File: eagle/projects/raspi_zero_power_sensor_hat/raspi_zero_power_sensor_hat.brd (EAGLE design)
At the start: 65 x 30 mm, 155 parts, among them J301 MOL-SL-2-RA, J302 USB_MICROB_RECPT, J401 MOL-SL-2-RA, J402 MOL-SL-2-V, J601 RECEPTACLE-2x5-2.54MM, J602 MOL-SL-4-RA, J603 MOL-SL-3-V, J604 RECEPTACLE-2x3-2.54MM, Q301 SSM6N7002KFU, Q401 SSM6N7002KFU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

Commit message: more routing
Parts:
- moved C401 0.10 mm to (16.0, 9.40)
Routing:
- net GND: track 113.4 -> 122.3 mm
- net USB_SHD: track 22.0 -> 13.5 mm
- net VBAT: track 0.00 -> 6.06 mm, vias 0 -> 3
- net VBAT_J: track 0.00 -> 5.49 mm
- net PP5V0_CHG_IN: track 5.60 -> 8.96 mm
- net I2C1_RASPI_SCL_R: track 16.5 -> 17.4 mm
- net TEMP_1WIRE_BI_R: track 24.6 -> 25.2 mm
- added copper zone on layer 2, net GND
- added copper zone on layer 1, net PP5V0_CHG_IN
- added copper zone on layer 1, net VBAT

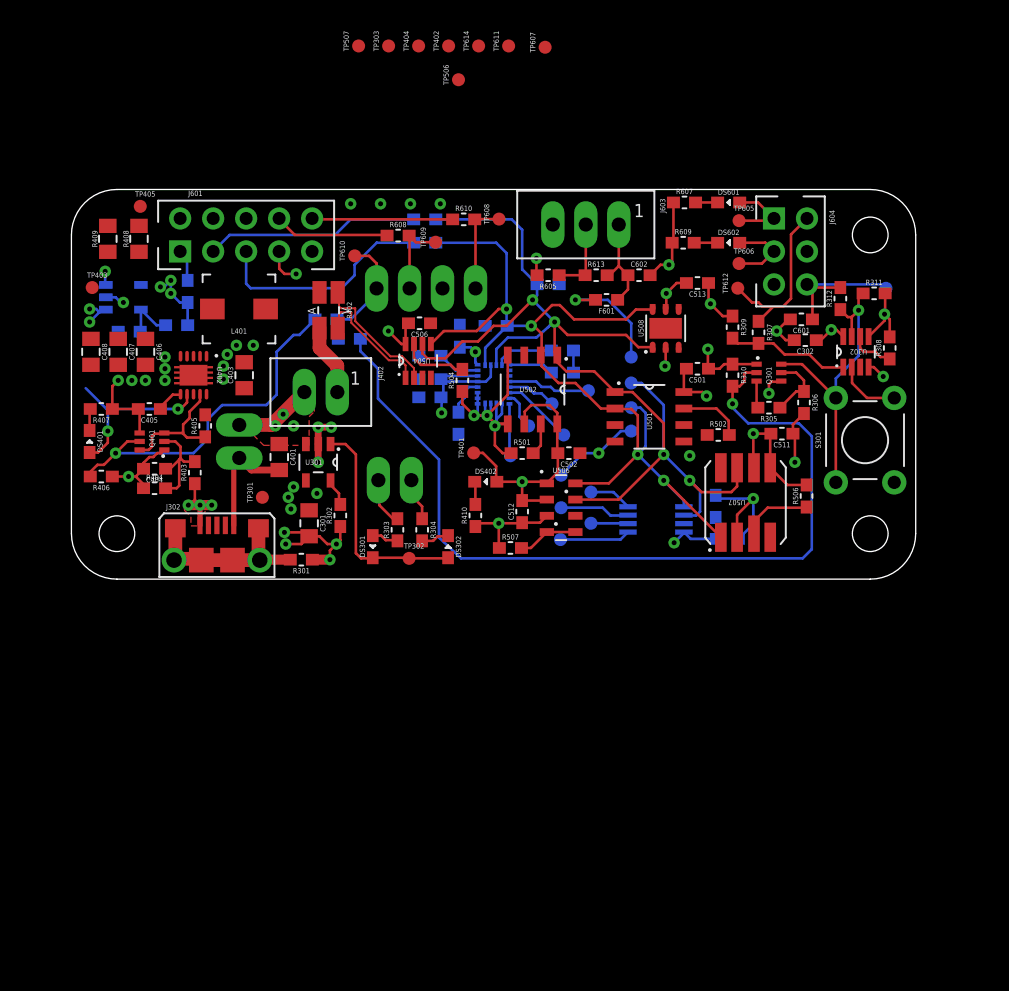
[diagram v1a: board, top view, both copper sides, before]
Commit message: almost done with routing. Move the ADC to north side to allow for I2C clip TPs
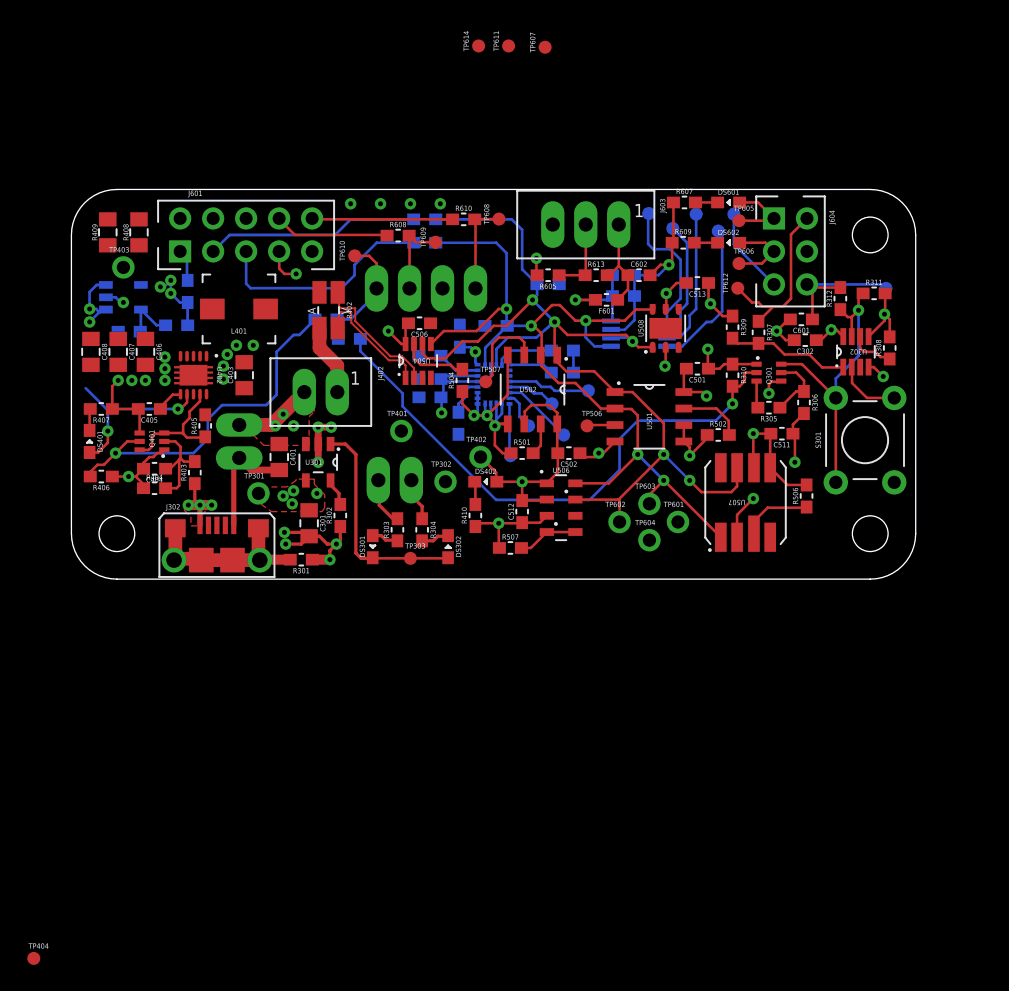
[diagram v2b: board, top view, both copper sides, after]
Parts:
- removed TP405: (no value), daqcs:TP10R
- TP301, TP302, TP401, TP402, TP403, TP601, TP602, TP603, TP604: device daqcs:TP10R -> daqcs:TP_TH102
- moved TP404 76.2 mm to (-2.90, -29.2), turned to 0 degrees
- moved TP303 39.5 mm to (26.1, 1.60), turned to 0 degrees
- moved TP402 31.7 mm to (31.5, 9.40), turned to 0 degrees
- moved TP506 28.4 mm to (39.7, 11.8), turned to 0 degrees
- moved TP507 27.6 mm to (31.9, 15.2), turned to 0 degrees
- moved TP504 26.0 mm to (44.5, 28.1)
- moved TP502 24.9 mm to (48.1, 28.1)
- moved TP505 24.1 mm to (51.0, 28.1)
- moved TP503 23.6 mm to (46.3, 27.0)
- moved TP501 22.4 mm to (49.8, 26.8)
- moved C504 21.8 mm to (42.5, 23.4)
- moved C503 17.7 mm to (42.5, 21.8), turned to 180 degrees
- moved U503 14.4 mm to (43.7, 18.9), turned to 0 degrees
- moved TP601 13.2 mm to (46.7, 4.40), flipped to the top, turned to 0 degrees
- moved TP602 10.7 mm to (42.2, 4.40), flipped to the top, turned to 0 degrees
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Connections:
- new net TEMP0_OS: TP506.TP, U501.3
- new net TEMP1_OS: TP507.TP, U502.3
- net CHG_STAT: now also TP303.TP; no longer TP302.TP
- net GND: now also TP302.1, TP604.1; no longer TP303.TP, TP402.TP, TP507.TP, TP604.TP
- net I2C1_RASPI_SCL: now also TP603.1; no longer TP603.TP
- net I2C1_RASPI_SDA: now also TP602.1; no longer TP602.TP
- net PP3V3_HAT: now also TP402.1, TP601.1; no longer TP401.TP, TP506.TP, TP601.TP
- net PP5V0_BST: now also TP403.1; no longer TP403.TP
- net PP5V0_BST_HAT: no longer TP405.TP
- net PP5V0_CHG_IN: now also TP301.1; no longer TP301.TP
- net VBAT_J: now also TP401.1
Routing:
- net MCU_TO_RASPI_RESET: track 67.4 -> 43.4 mm
- net GND: track 122.3 -> 131.7 mm
- net ADC_AIN3_REF: track 3.32 -> 11.7 mm
- net PP3V3_HAT: track 83.7 -> 76.2 mm, vias 15 -> 14
- net I2C1_RASPI_SDA: track 85.1 -> 77.5 mm, vias 4 -> 5
- net TEMP1_OS: track 0.00 -> 6.92 mm
- net ADC_AIN1: track 2.86 -> 9.27 mm
- net ADC_AIN2: track 5.41 -> 11.0 mm
- net ADC_AIN0: track 5.44 -> 10.5 mm
- net TEMP0_OS: track 0.00 -> 2.18 mm
- net PP5V0_BST: track 17.2 -> 18.9 mm, vias 5 -> 4
- net I2C1_RASPI_SCL: track 72.5 -> 70.9 mm, vias 4 -> 5
- net CHG_STAT: track 17.2 -> 18.1 mm
- added copper zone on layer 15, net PP5V0_CHG_IN

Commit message: working on power layout
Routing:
- net VBAT_R: track 0.00 -> 4.72 mm
- net MCU_TO_BST_RESET: track 27.7 -> 26.8 mm
- net GND: track 131.7 -> 131.6 mm, vias 38 -> 42
- added copper zone on layer 1, net BST_SW
- added copper zone on layer 1, net GND
- added copper zone on layer 16, net GND
- added copper zone on layer 16, net PP5V0_CHG_IN
- added copper zone on layer 16, net VBAT
- added copper zone on layer 1, net VBAT_R

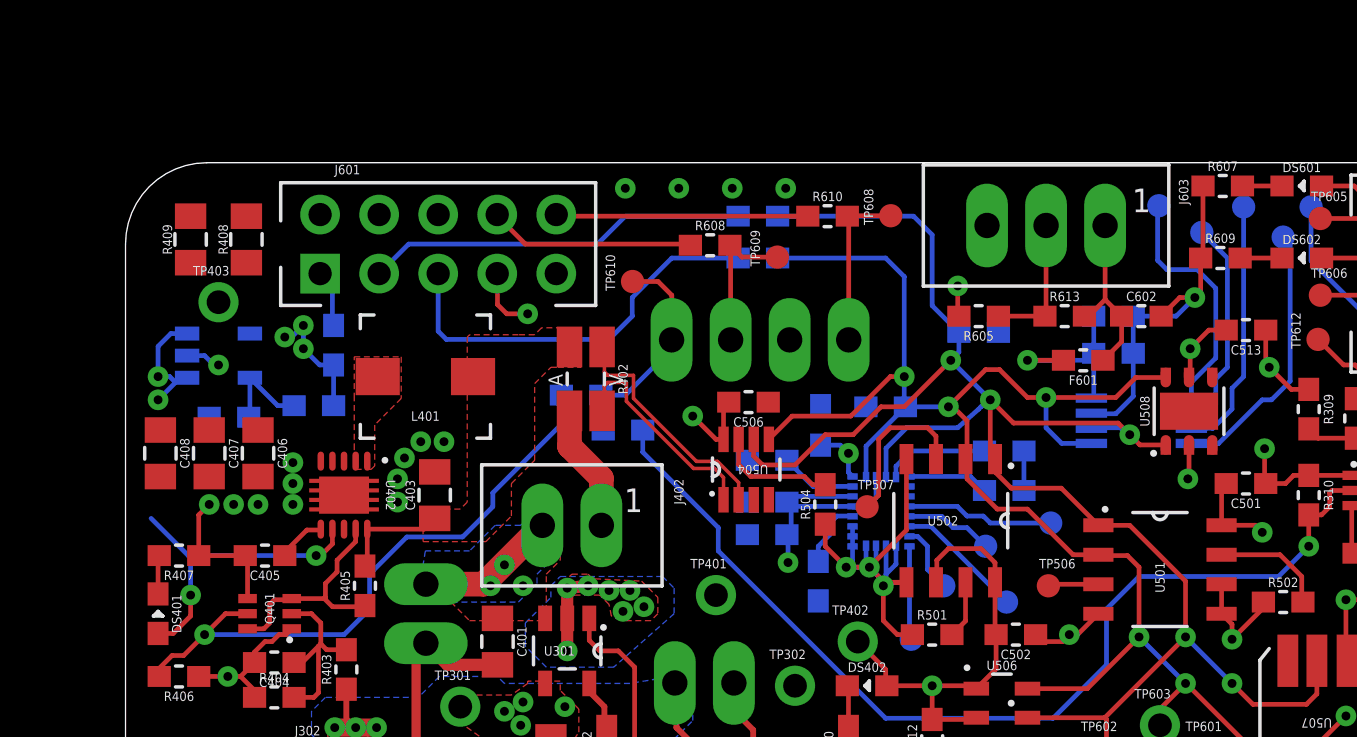
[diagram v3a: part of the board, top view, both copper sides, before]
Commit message: more routing and power planing. move the I2C series resisters after the nostuff pullups. Needed to do this because I placed them under a connector :)
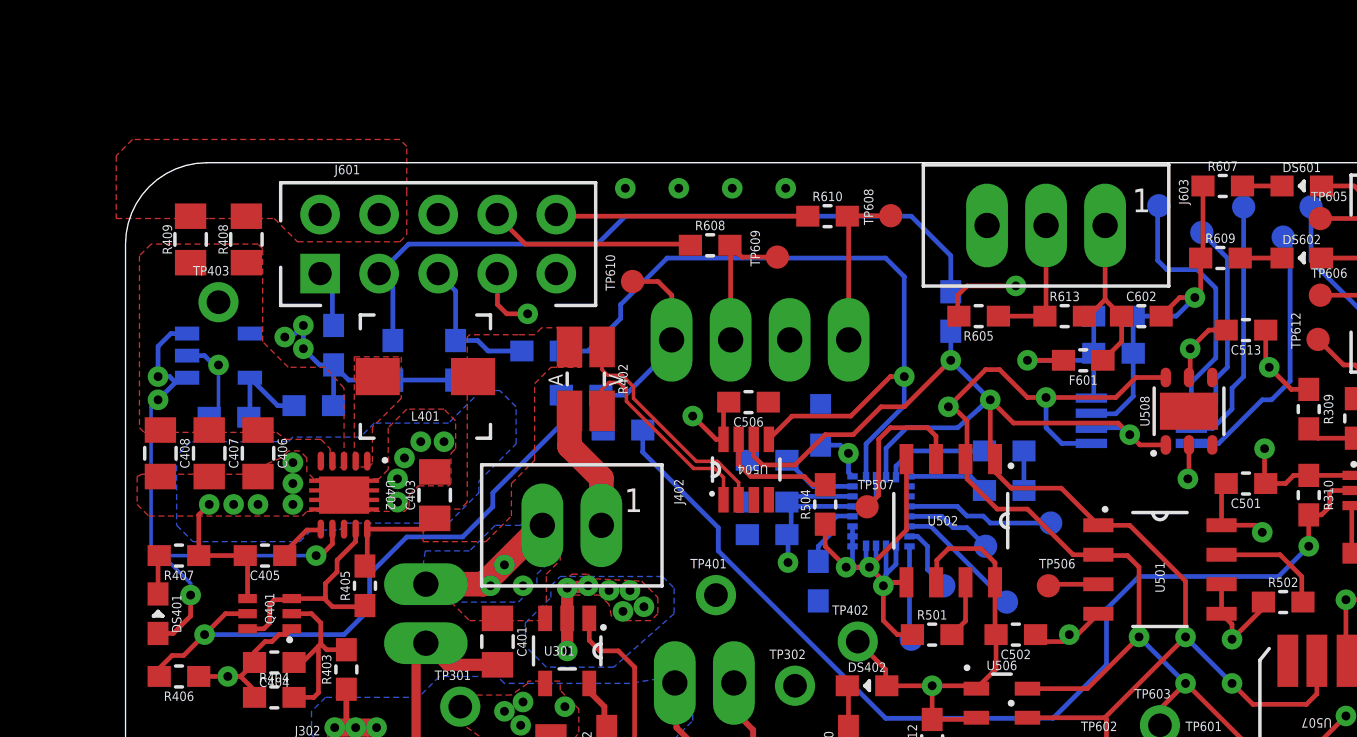
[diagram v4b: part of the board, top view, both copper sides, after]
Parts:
- moved R602 22.5 mm to (14.2, 21.5), turned to 270 degrees
- moved R601 21.3 mm to (11.5, 21.5), turned to 270 degrees
- moved R603 10.1 mm to (17.9, 21.9)
- moved R604 9.26 mm to (35.5, 23.6), turned to 90 degrees
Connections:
- net I2C1_RASPI_SCL: no longer R601.1
- net I2C1_RASPI_SCL_R: now also R602.1
- net I2C1_RASPI_SDA: no longer R602.1
- net I2C1_RASPI_SDA_R: now also R601.1
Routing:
- net I2C1_RASPI_SDA_R: track 16.5 -> 31.0 mm
- net I2C1_RASPI_SDA: track 77.5 -> 65.7 mm
- net I2C1_RASPI_SCL_R: track 17.4 -> 6.23 mm
- net I2C1_RASPI_SCL: track 70.9 -> 80.3 mm
- net PP5V0_BST: track 18.9 -> 25.3 mm
- net PP3V3_HAT: track 76.2 -> 81.7 mm
- net TEMP_1WIRE_BI_R: track 25.2 -> 30.0 mm
- net GND: track 131.6 -> 134.0 mm
- added copper zone on layer 1, net PP5V0_BST
- added copper zone on layer 1, net PP5V0_BST_HAT

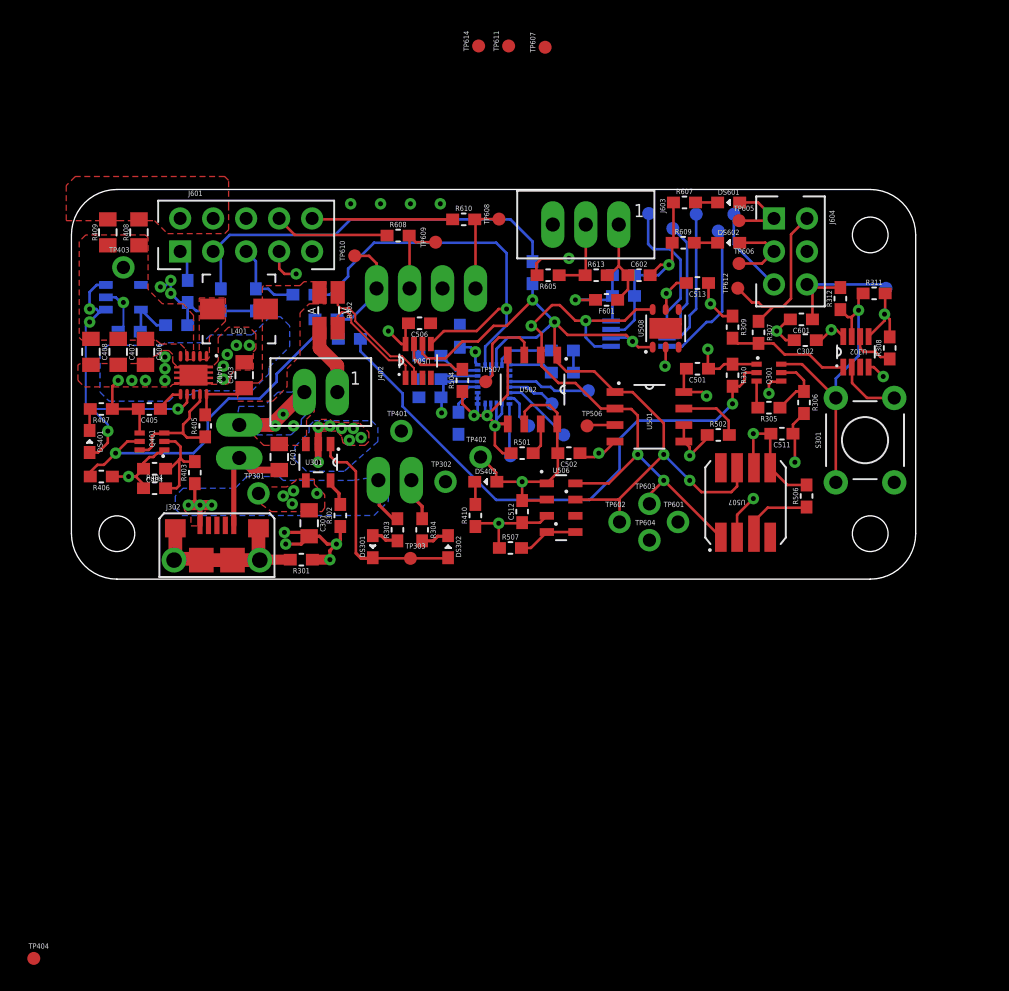
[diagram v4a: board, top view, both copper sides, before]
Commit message: ALL FUCKING ROUTED... W00T. still need TO DO: adjust trace widths for max allowed. Touch up power planes. place/replace some TPs. FIX THE SILK LAYERS / name / value. Adjust silk on RA SL
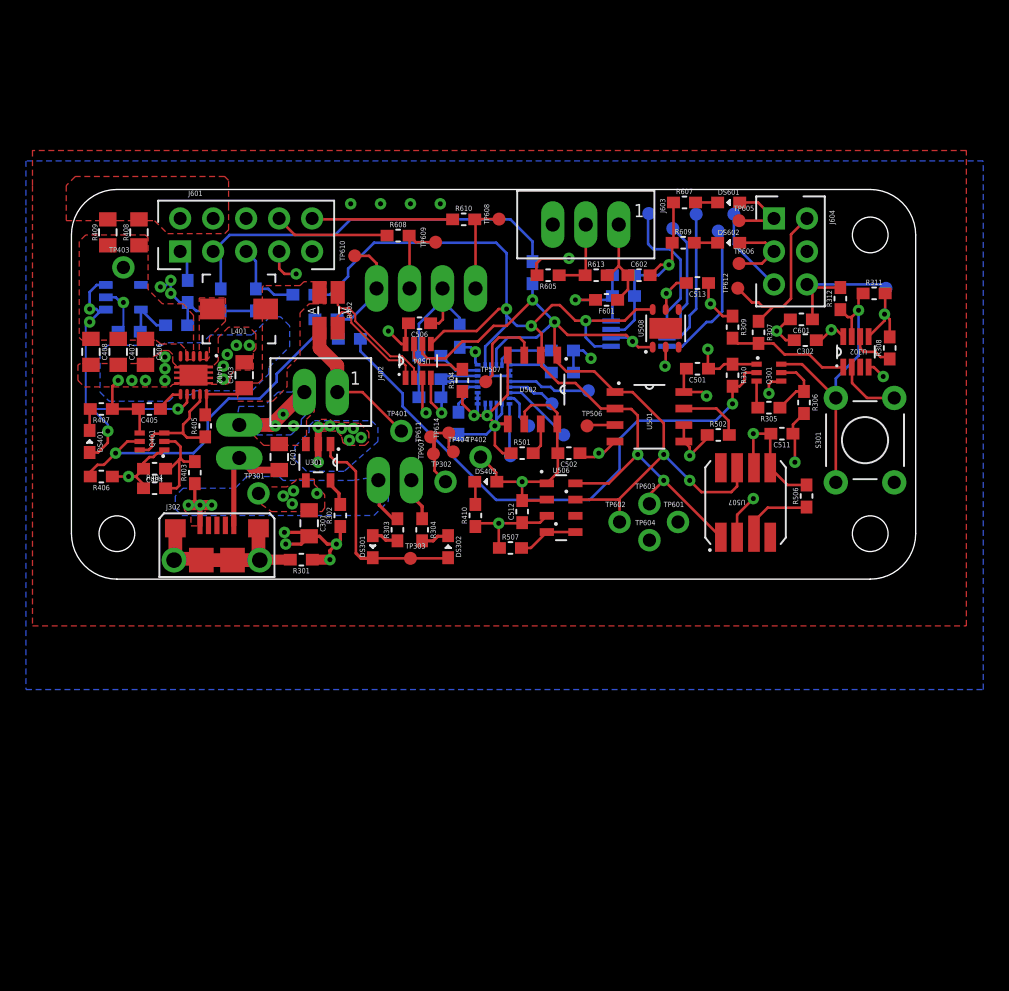
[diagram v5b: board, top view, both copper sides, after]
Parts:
- moved TP404 50.6 mm to (29.4, 9.80)
- moved TP607 32.5 mm to (27.9, 9.65)
- moved TP611 30.7 mm to (27.7, 10.9)
- moved TP614 29.9 mm to (29.1, 11.2)
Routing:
- net GND: track 134.0 -> 166.1 mm, vias 42 -> 44
- net VBAT_J: track 5.49 -> 11.7 mm
- net PP3V3_HAT: track 81.7 -> 86.6 mm
- net I2C1_RASPI_SCL: track 80.3 -> 82.6 mm
- net USB_SHD: track 13.5 -> 14.1 mm
- added copper zone on layer 15, net PP3V3_HAT

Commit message: fixed up poly isolation. changed all traces to 10mil width except for current sense on the TOP and IMU trace on the bottom
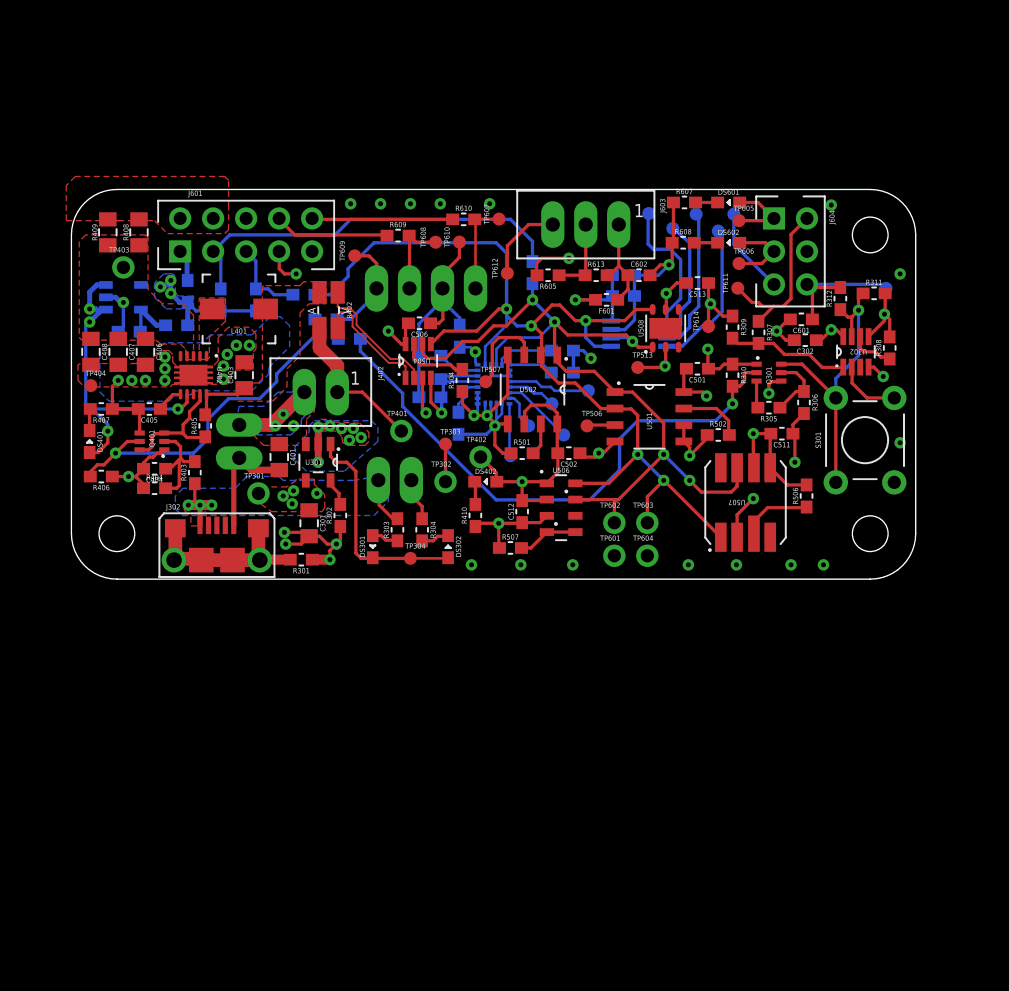
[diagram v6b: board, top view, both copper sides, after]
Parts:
- added TP304, TP513: (no value), daqcs:TP10R
- R601, R602, R609: value 2k -> 0.0
- R603, R604, R608: value 0.0 -> 2k
- moved TP404 28.4 mm to (1.50, 14.9)
- moved TP611 26.3 mm to (51.3, 22.4)
- moved R601 24.1 mm to (35.5, 23.6), turned to 90 degrees
- moved R608 22.0 mm to (47.1, 25.9)
- moved R609 22.0 mm to (25.1, 26.4)
- moved TP614 21.6 mm to (49.0, 19.4)
- moved R604 21.4 mm to (14.2, 21.5), turned to 270 degrees
- moved TP607 18.8 mm to (32.9, 27.7)
- moved TP612 17.8 mm to (33.6, 23.6)
- moved TP303 9.20 mm to (28.8, 10.4)
- moved TP610 8.13 mm to (29.9, 25.9)
- moved R603 6.41 mm to (11.5, 21.5), turned to 270 degrees
- moved TP609 6.32 mm to (21.8, 24.9)
- moved TP601 5.55 mm to (41.8, 1.80)
- moved TP608 5.19 mm to (28.0, 25.9)
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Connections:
- net CHG_STAT: now also TP304.TP; no longer TP303.TP
- net DBG_LED1: now also R608.2; no longer R609.2
- net GND: now also R608.1, TP303.TP, TP513.TP, TP610.TP, TP612.TP; no longer R609.1, TP607.TP, TP611.TP
- net I2C1_RASPI_SCL: now also R602.1; no longer R603.1
- net I2C1_RASPI_SCL_R: now also R602.2, R604.1; no longer R602.1, R603.2
- net I2C1_RASPI_SDA: now also R601.1; no longer R604.1
- net I2C1_RASPI_SDA_R: now also R601.2, R603.1; no longer R601.1, R604.2
- net MCU_TO_HAT_RESET: now also TP609.TP; no longer TP610.TP
- net PP3V3_HAT: now also R603.2, R604.2; no longer R601.2, R602.2
- net UART_RASPI_RXD_MCU_TXD: now also TP607.TP; no longer TP608.TP
- net UART_RASPI_TXD_MCU_RXD: now also R609.2, TP608.TP; no longer R608.2, TP609.TP
- net UART_RASPI_TXD_MCU_RXD_R: now also R609.1; no longer R608.1
- net WDT_PET_R: now also TP611.TP; no longer TP612.TP
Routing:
- net GND: track 166.1 -> 174.8 mm, vias 44 -> 55
- net I2C1_RASPI_SCL: track 82.6 -> 84.1 mm
- added copper zone on layer 16, net PP3V3_HAT
